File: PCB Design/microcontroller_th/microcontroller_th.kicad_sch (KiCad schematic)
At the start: 9 parts, among them CN2 1X4SMT, U1 ATmega328P-P, Y1 Crystal_Small

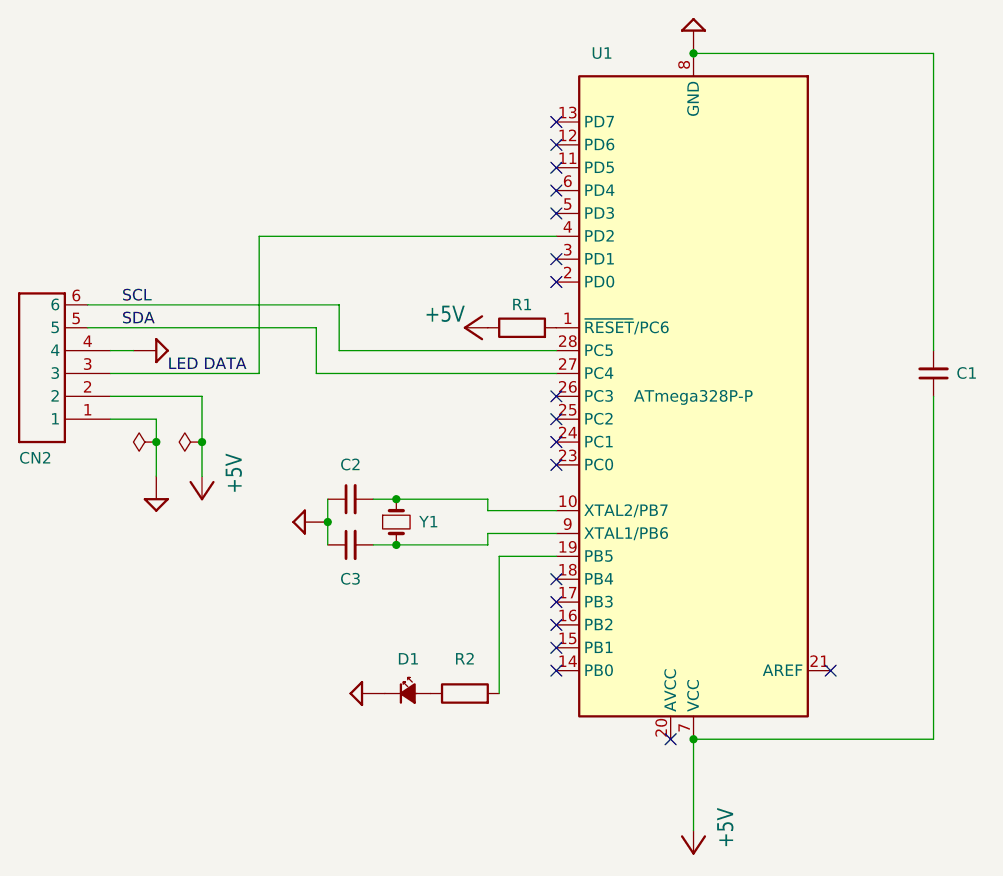
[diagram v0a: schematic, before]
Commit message: atmega reset
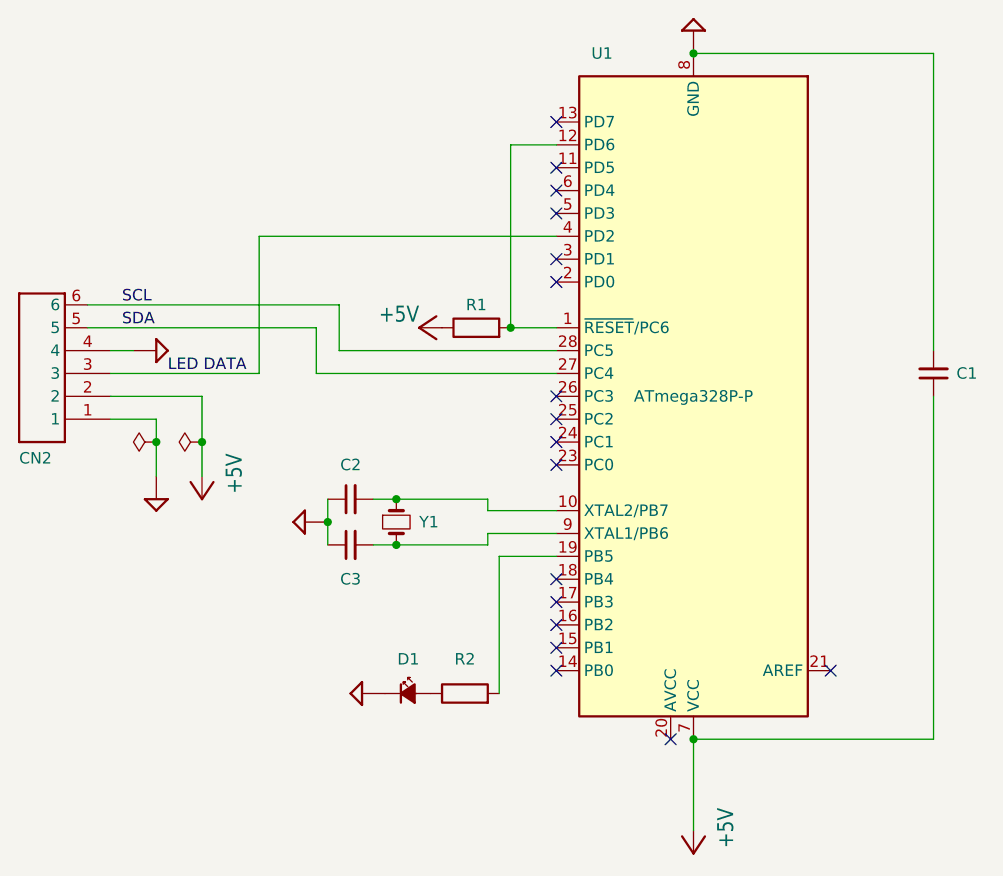
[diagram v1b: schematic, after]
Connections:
- net at R1.2, U1.1 (~{RESET}/PC6): now also U1.12 (PD6)
- no-connect marks 18 -> 17
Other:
- moved on the sheet: R1
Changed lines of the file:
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@@
   (junction (at 45.72 129.54) (diameter 0) (color 0 0 0 0)
+  )
+  (junction (at 85.09 116.84) (diameter 0) (color 0 0 0 0)
   )
   (junction (at 105.41 162.56) (diameter 0) (color 0 0 0 0)
@@
   (no_connect (at 102.87 162.56))
   (no_connect (at 90.17 93.98))
-  (no_connect (at 90.17 96.52))
   (no_connect (at 90.17 99.06))
   (no_connect (at 90.17 101.6))
@@
     (stroke (width 0) (type default) (color 0 0 0 0))
   )
+  (wire (pts (xy 85.09 116.84) (xy 90.17 116.84))
+    (stroke (width 0) (type default) (color 0 0 0 0))
+  )
   (wire (pts (xy 82.55 139.7) (xy 90.17 139.7))
     (stroke (width 0) (type default) (color 0 0 0 0))
   )
+  (wire (pts (xy 85.09 96.52) (xy 85.09 116.84))
+    (stroke (width 0) (type default) (color 0 0 0 0))
+  )
   (wire (pts (xy 64.77 138.43) (xy 64.77 140.97))
     (stroke (width 0) (type default) (color 0 0 0 0))
@@
   )
   (wire (pts (xy 90.17 142.24) (xy 83.82 142.24))
+    (stroke (width 0) (type default) (color 0 0 0 0))
+  )
+  (wire (pts (xy 90.17 96.52) (xy 85.09 96.52))
     (stroke (width 0) (type default) (color 0 0 0 0))
   )
@@
     (pin "1")
   )
-  (symbol (lib_id "Adafruit NeoPixel 8 Stick-eagle-import:+5V") (at 80.01 116.84 90) (unit 1)
-    (in_bom yes) (on_board yes)
-    (property "Reference" "#P+0103" (id 0) (at 80.01 116.84 0)
-      (effects (font (size 1.27 1.27)) hide)
-    )
-    (property "Value" "+5V" (id 1) (at 80.01 114.3 90)
+  (symbol (lib_id "Adafruit NeoPixel 8 Stick-eagle-import:+5V") (at 74.93 116.84 90) (unit 1)
+    (in_bom yes) (on_board yes)
+    (property "Reference" "#P+0103" (id 0) (at 74.93 116.84 0)
+      (effects (font (size 1.27 1.27)) hide)
+    )
+    (property "Value" "+5V" (id 1) (at 74.93 114.3 90)
       (effects (font (size 1.778 1.5113)) (justify left bottom))
     )
-    (property "Footprint" "Adafruit NeoPixel 8 Stick:" (id 2) (at 80.01 116.84 0)
-      (effects (font (size 1.27 1.27)) hide)
-    )
-    (property "Datasheet" "" (id 3) (at 80.01 116.84 0)
+    (property "Footprint" "Adafruit NeoPixel 8 Stick:" (id 2) (at 74.93 116.84 0)
+      (effects (font (size 1.27 1.27)) hide)
+    )
+    (property "Datasheet" "" (id 3) (at 74.93 116.84 0)
       (effects (font (size 1.27 1.27)) hide)
     )
@@
     (pin "1")
   )
-  (symbol (lib_id "Device:R") (at 86.36 116.84 90) (unit 1)
-    (in_bom yes) (on_board yes)
-    (property "Reference" "R1" (id 0) (at 86.36 114.3 90))
-    (property "Value" "R" (id 1) (at 86.36 113.03 90)
-      (effects (font (size 1.27 1.27)) hide)
-    )
-    (property "Footprint" "Resistor_THT:R_Axial_DIN0207_L6.3mm_D2.5mm_P7.62mm_Horizontal" (id 2) (at 86.36 118.618 90)
-      (effects (font (size 1.27 1.27)) hide)
-    )
-    (property "Datasheet" "~" (id 3) (at 86.36 116.84 0)
-      (effects (font (size 1.27 1.27)) hide)
-    )
+  (symbol (lib_id "Device:R") (at 81.28 116.84 90) (unit 1)
+    (in_bom yes) (on_board yes)
+    (property "Reference" "R1" (id 0) (at 81.28 114.3 90))
+    (property "Value" "R" (id 1) (at 81.28 113.03 90)
+      (effects (font (size 1.27 1.27)) hide)
+    )
+    (property "Footprint" "Resistor_THT:R_Axial_DIN0207_L6.3mm_D2.5mm_P7.62mm_Horizontal" (id 2) (at 81.28 118.618 90)
+      (effects (font (size 1.27 1.27)) hide)
+    )
+    (property "Datasheet" "~" (id 3) (at 81.28 116.84 0)
+      (effects (font (size 1.27 1.27)) hide)
+    )
